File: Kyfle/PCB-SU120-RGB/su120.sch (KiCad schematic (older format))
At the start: 79 parts, among them J1 MJ-4PP-9, J2 Conn_01x03, J3 Conn_01x08, J4 Conn_01x08, J6 MJ-4PP-9, J7 Conn_02x05_Odd_Even, J8 Conn_02x05_Odd_Even, SW1 SW_PUSH_LED, SW10 SW_PUSH_LED, SW11 SW_PUSH_LED, SW12 SW_PUSH_LED, SW13 SW_PUSH_LED, SW14 SW_PUSH_LED, SW15 SW_PUSH_LED, SW16 SW_PUSH_LED, SW17 SW_PUSH_LED, SW18 SW_PUSH_LED, SW2 SW_PUSH_LED, SW20 Rotary_Encoder_Switch, SW21 Rotary_Encoder_Switch, SW22 SW_Push, SW3 SW_PUSH_LED, SW4 SW_PUSH_LED, SW5 SW_PUSH_LED, SW6 SW_PUSH_LED, SW7 SW_PUSH_LED, SW8 SW_PUSH_LED, SW9 SW_PUSH_LED, U1 ProMicro

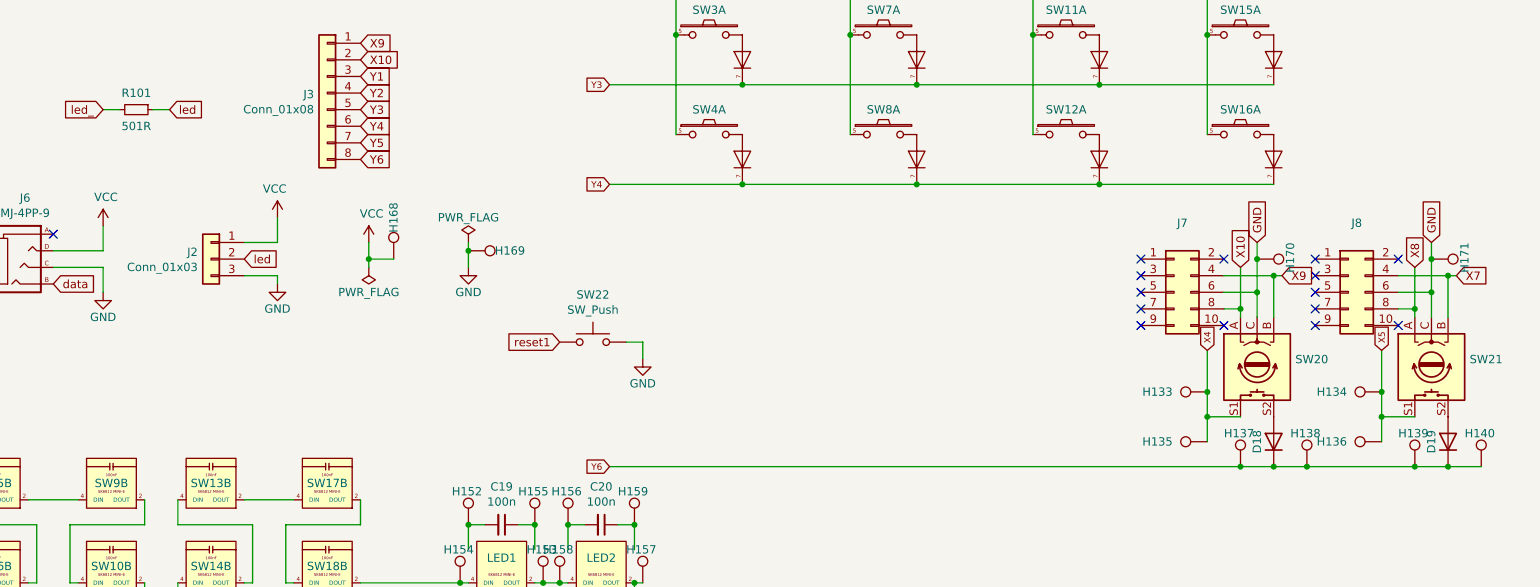
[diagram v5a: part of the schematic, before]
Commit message: PCB done. Started redoing the rails.
- PCB should be in its final version now, pretty much. I hope...
- I added a tentative compatibility with Panasonic roller encoders.
- Also added some silk screens for the 2u stabilisers.
- Propagated the new bit board design to footprints used for top and bottom plate.
- And started to rework the rails in the bottom plate, as well as the general shape of the keyboard.
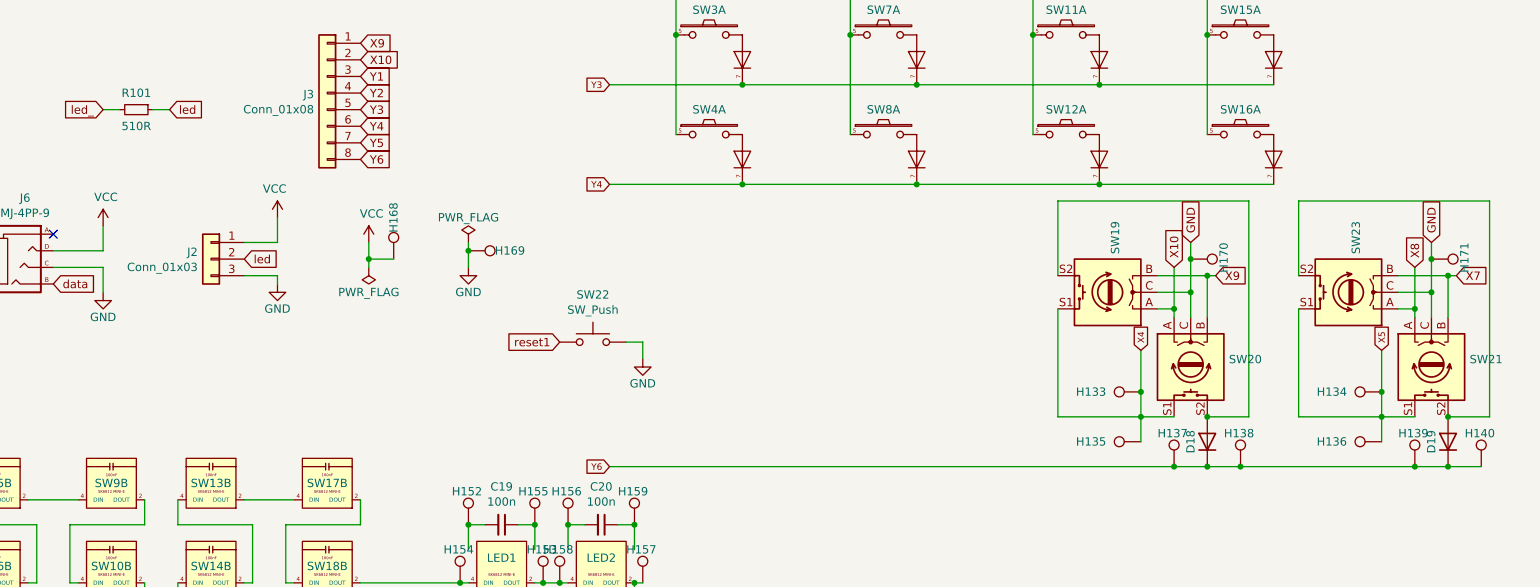
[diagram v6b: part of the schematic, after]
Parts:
- removed J7, J8: Conn_02x05_Odd_Even, #footprint:IDC-Header_2x05_P2.54mm_Vertical, symbol Connector_Generic:Conn_02x05_Odd_Even
- added SW19, SW23: Rotary_Encoder_Switch, Kyfle Footprints:RollerEncoder_Panasonic_EVQWGD001, symbol Device:Rotary_Encoder_Switch
- R101: value 501R -> 510R
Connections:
- net GND: now also SW19.C, SW23.C
- net X10: now also SW19.A
- net X4: now also SW19.S1
- net X5: now also SW23.S1
- net X7: now also SW23.B
- net X8: now also SW23.A
- net X9: now also SW19.B
- net at D18.2 (A), SW20.S2: now also SW19.S2
- net at D19.2 (A), SW21.S2: now also SW23.S2
- no-connect marks 18 -> 4
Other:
- moved on the sheet: D18, H133, H135, H137, H138, H170, SW20
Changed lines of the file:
@@
 L Device:D D18
 U 1 1 5CE5B1E1
-P 9600 5350
-F 0 "D18" H 9600 5450 50  0000 C CNN
-F 1 "D" H 9600 5250 50  0001 C CNN
-F 2 "#footprint:diode_TH_SMD_rev2" H 9600 5350 50  0001 C CNN
-F 3 "" H 9600 5350 50  0001 C CNN
-	1    9600 5350
+P 9200 5350
+F 0 "D18" H 9200 5450 50  0000 C CNN
+F 1 "D" H 9200 5250 50  0001 C CNN
+F 2 "#footprint:diode_TH_SMD_rev2" H 9200 5350 50  0001 C CNN
+F 3 "" H 9200 5350 50  0001 C CNN
+	1    9200 5350
 	0    -1   -1   0
 $EndComp
@@
 Text GLabel 8150 800  1    39   Input ~ 0
 X3
-Text GLabel 9200 4800 1    39   Input ~ 0
+Text GLabel 8800 4800 1    39   Input ~ 0
 X4
 Text GLabel 10250 4800 1    39   Input ~ 0
 X5
-Connection ~ 9600 5500
-Wire Wire Line
-	9600 5500 9800 5500
+Connection ~ 9200 5500
+Wire Wire Line
+	9200 5500 9400 5500
 $Comp
 L Connector:TestPoint H137
 U 1 1 5CE5B292
+P 9000 5500
+F 0 "H137" H 8900 5700 50  0000 L CNN
+F 1 "MountingHole_Pad" H 9100 5460 50  0001 L CNN
+F 2 "#footprint:1pad_conn" H 9000 5500 50  0001 C CNN
+F 3 "~" H 9000 5500 50  0001 C CNN
+	1    9000 5500
+	1    0    0    -1
+$EndComp
+Connection ~ 9000 5500
+Wire Wire Line
+	9000 5500 9200 5500
+$Comp
+L Connector:TestPoint H138
+U 1 1 5CE5B29A
 P 9400 5500
-F 0 "H137" H 9300 5700 50  0000 L CNN
+F 0 "H138" H 9300 5700 50  0000 L CNN
 F 1 "MountingHole_Pad" H 9500 5460 50  0001 L CNN
 F 2 "#footprint:1pad_conn" H 9400 5500 50  0001 C CNN
@@
 Connection ~ 9400 5500
 Wire Wire Line
-	9400 5500 9600 5500
-$Comp
-L Connector:TestPoint H138
-U 1 1 5CE5B29A
-P 9800 5500
-F 0 "H138" H 9700 5700 50  0000 L CNN
-F 1 "MountingHole_Pad" H 9900 5460 50  0001 L CNN
-F 2 "#footprint:1pad_conn" H 9800 5500 50  0001 C CNN
-F 3 "~" H 9800 5500 50  0001 C CNN
-	1    9800 5500
-	1    0    0    -1
-$EndComp
-Connection ~ 9800 5500
-Wire Wire Line
-	9800 5500 10450 5500
+	9400 5500 10450 5500
 $Comp
 L Connector:TestPoint H139
@@
 	1    0    0    -1
 $EndComp
-Connection ~ 10450 5500
-Wire Wire Line
-	10450 5500 10650 5500
 $Comp
 L Connector:TestPoint H140
@@
 L Connector:TestPoint H133
 U 1 1 5CE5B2B0
-P 9200 5050
-F 0 "H133" V 9200 5350 50  0000 C CNN
-F 1 "MountingHole_Pad" V 9346 5055 50  0001 C CNN
-F 2 "#footprint:1pad_conn" H 9200 5050 50  0001 C CNN
-F 3 "~" H 9200 5050 50  0001 C CNN
-	1    9200 5050
+P 8800 5050
+F 0 "H133" V 8800 5350 50  0000 C CNN
+F 1 "MountingHole_Pad" V 8946 5055 50  0001 C CNN
+F 2 "#footprint:1pad_conn" H 8800 5050 50  0001 C CNN
+F 3 "~" H 8800 5050 50  0001 C CNN
+	1    8800 5050
 	0    -1   -1   0
 $EndComp
-Connection ~ 9200 5050
+Connection ~ 8800 5050
 $Comp
 L Connector:TestPoint H135
 U 1 1 5CE5B2B8
-P 9200 5350
-F 0 "H135" V 9200 5650 50  0000 C CNN
-F 1 "MountingHole_Pad" V 9346 5355 50  0001 C CNN
-F 2 "#footprint:1pad_conn" H 9200 5350 50  0001 C CNN
-F 3 "~" H 9200 5350 50  0001 C CNN
-	1    9200 5350
+P 8800 5350
+F 0 "H135" V 8800 5650 50  0000 C CNN
+F 1 "MountingHole_Pad" V 8946 5355 50  0001 C CNN
+F 2 "#footprint:1pad_conn" H 8800 5350 50  0001 C CNN
+F 3 "~" H 8800 5350 50  0001 C CNN
+	1    8800 5350
 	0    -1   -1   0
 $EndComp
@@
 $EndComp
 Wire Wire Line
-	5600 5500 9400 5500
+	5600 5500 9000 5500
 Wire Wire Line
 	10250 4800 10250 5050
 Wire Wire Line
-	9200 4800 9200 5050
-Wire Wire Line
-	9200 5050 9200 5200
+	8800 4800 8800 5050
+Wire Wire Line
+	8800 5050 8800 5200
 Wire Wire Line
 	10250 5050 10250 5200
-$Comp
-L Device:Rotary_Encoder_Switch SW20
-U 1 1 5D659111
-P 9500 4900
-F 0 "SW20" V 9454 4670 50  0000 R CNN
-F 1 "Rotary_Encoder_Switch" V 9545 4670 50  0001 R CNN
-F 2 "#footprint:RotaryEncoder_Alps_EC11E-Switch_Vertical_H20mm_rev2" H 9350 5060 50  0001 C CNN
-F 3 "~" H 9500 5160 50  0001 C CNN
-	1    9500 4900
-	0    -1   1    0
-$EndComp
 $Comp
 L Device:Rotary_Encoder_Switch SW21
@@
 $EndComp
 Wire Wire Line
-	9400 5200 9200 5200
-Connection ~ 9200 5200
-Wire Wire Line
-	9200 5200 9200 5350
+	9000 5200 8800 5200
+Connection ~ 8800 5200
+Wire Wire Line
+	8800 5200 8800 5350
 Wire Wire Line
 	10450 5200 10250 5200
@@
 Wire Wire Line
 	10250 5200 10250 5350
-Text GLabel 9500 4150 1    50   Input ~ 0
+Text GLabel 9100 4150 1    50   Input ~ 0
 GND
 Text GLabel 10550 4150 1    50   Input ~ 0
@@
 	1    0    0    -1
 $EndComp
-$Comp
-L Connector_Generic:Conn_02x05_Odd_Even J8
-U 1 1 5E124F08
-P 10050 4450
-F 0 "J8" H 10100 4867 50  0000 C CNN
-F 1 "Conn_02x05_Odd_Even" H 10100 4776 50  0001 C CNN
-F 2 "#footprint:IDC-Header_2x05_P2.54mm_Vertical" H 10050 4450 50  0001 C CNN
-F 3 "~" H 10050 4450 50  0001 C CNN
-	1    10050 4450
-	1    0    0    -1
-$EndComp
-$Comp
-L Connector_Generic:Conn_02x05_Odd_Even J7
-U 1 1 5E113B23
-P 9000 4450
-F 0 "J7" H 9050 4867 50  0000 C CNN
-F 1 "Conn_02x05_Odd_Even" H 9050 4776 50  0001 C CNN
-F 2 "#footprint:IDC-Header_2x05_P2.54mm_Vertical" H 9000 4450 50  0001 C CNN
-F 3 "~" H 9000 4450 50  0001 C CNN
-	1    9000 4450
-	1    0    0    -1
-$EndComp
-Wire Wire Line
-	9400 4300 9400 4550
-Wire Wire Line
-	9500 4150 9500 4250
+Wire Wire Line
+	9000 4300 9000 4550
+Wire Wire Line
+	9100 4150 9100 4250
 Wire Wire Line
 	10450 4300 10450 4550
@@
 	10550 4150 10550 4250
 Wire Wire Line
-	9300 4350 9600 4350
-Wire Wire Line
-	9600 4350 9600 4600
-Wire Wire Line
-	9300 4450 9500 4450
-Connection ~ 9500 4450
-Wire Wire Line
-	9500 4450 9500 4600
-Wire Wire Line
-	9300 4550 9400 4550
-Connection ~ 9400 4550
-Wire Wire Line
-	9400 4550 9400 4600
+	8900 4350 9200 4350
+Wire Wire Line
+	9200 4350 9200 4600
+Wire Wire Line
+	8900 4450 9100 4450
+Connection ~ 9100 4450
+Wire Wire Line
+	9100 4450 9100 4600
+Wire Wire Line
+	8900 4550 9000 4550
+Connection ~ 9000 4550
+Wire Wire Line
+	9000 4550 9000 4600
 Wire Wire Line
 	10350 4350 10650 4350
@@
 	1    0    0    -1
 $EndComp
-NoConn ~ 8800 4250
-NoConn ~ 8800 4350
-NoConn ~ 8800 4450
-NoConn ~ 8800 4550
-NoConn ~ 8800 4650
-NoConn ~ 9300 4650
-NoConn ~ 9300 4250
-NoConn ~ 9850 4250
-NoConn ~ 9850 4350
-NoConn ~ 9850 4450
-NoConn ~ 9850 4550
-NoConn ~ 9850 4650
-NoConn ~ 10350 4650
-NoConn ~ 10350 4250
 $Comp
 L Sofle:SW_PUSH_LED SW4
@@
 P 2750 3350
 F 0 "R101" V 2650 3350 50  0000 C CNN
-F 1 "501R" V 2850 3350 50  0000 C CNN
+F 1 "510R" V 2850 3350 50  0000 C CNN
 F 2 "Resistor_SMD:R_0603_1608Metric_Pad0.98x0.95mm_HandSolder" H 2750 3350 50  0001 C CNN
 F 3 "~" H 2750 3350 50  0001 C CNN
@@
 Wire Wire Line
 	2650 3350 2550 3350
-Connection ~ 9600 4350
+Connection ~ 9200 4350
 Wire Wire Line
 	10700 4350 10650 4350
@@
 L Connector:TestPoint H170
 U 1 1 617932EC
-P 9500 4250
-F 0 "H170" H 9400 4450 50  0000 L CNN
-F 1 "MountingHole_Pad" H 9600 4210 50  0001 L CNN
-F 2 "#footprint:1pin_conn" H 9500 4250 50  0001 C CNN
-F 3 "~" H 9500 4250 50  0001 C CNN
-	1    9500 4250
+P 9100 4250
+F 0 "H170" H 9000 4450 50  0000 L CNN
+F 1 "MountingHole_Pad" H 9200 4210 50  0001 L CNN
+F 2 "#footprint:1pin_conn" H 9100 4250 50  0001 C CNN
+F 3 "~" H 9100 4250 50  0001 C CNN
+	1    9100 4250
 	0    1    1    0
 $EndComp
-Connection ~ 9500 4250
-Wire Wire Line
-	9500 4250 9500 4450
+Connection ~ 9100 4250
+Wire Wire Line
+	9100 4250 9100 4450
 $Comp
 L Connector:TestPoint H171
@@
 	4750 4200 4750 4300
 Wire Wire Line
-	9650 4350 9600 4350
-Text GLabel 9650 4350 2    50   Input ~ 0
-X9
-Text GLabel 9400 4300 1    50   Input ~ 0
+	9250 4350 9200 4350
+Text GLabel 9000 4300 1    50   Input ~ 0
 X10
 Text GLabel 3450 1900 2    50   Input ~ 0
@@
 Text GLabel 3400 4250 2    50   Input ~ 0
 led
+$Comp
+L Device:Rotary_Encoder_Switch SW20
+U 1 1 5D659111
+P 9100 4900
+F 0 "SW20" V 9054 4670 50  0000 R CNN
+F 1 "Rotary_Encoder_Switch" V 9145 4670 50  0001 R CNN
+F 2 "#footprint:RotaryEncoder_Alps_EC11E-Switch_Vertical_H20mm_rev2" H 8950 5060 50  0001 C CNN
+F 3 "~" H 9100 5160 50  0001 C CNN
+	1    9100 4900
+	0    -1   1    0
+$EndComp
+Text GLabel 9250 4350 2    50   Input ~ 0
+X9
+$Comp
+L Device:Rotary_Encoder_Switch SW19
+U 1 1 617B91CB
+P 8600 4450
+F 0 "SW19" V 8554 4220 50  0000 R CNN
+F 1 "Rotary_Encoder_Switch" V 8645 4220 50  0001 R CNN
+F 2 "Kyfle Footprints:RollerEncoder_Panasonic_EVQWGD001" H 8450 4610 50  0001 C CNN
+F 3 "~" H 8600 4710 50  0001 C CNN
+	1    8600 4450
+	-1   0    0    1
+$EndComp
+Wire Wire Line
+	8300 4550 8300 5200
+Wire Wire Line
+	8300 5200 8800 5200
+Connection ~ 9200 5200
+Wire Wire Line
+	8300 4350 8300 3900
+Wire Wire Line
+	8300 3900 9450 3900
+Wire Wire Line
+	9450 3900 9450 5200
+Wire Wire Line
+	9450 5200 9200 5200
+$Comp
+L Device:Rotary_Encoder_Switch SW23
+U 1 1 617D6B8F
+P 10050 4450
+F 0 "SW23" V 10004 4220 50  0000 R CNN
+F 1 "Rotary_Encoder_Switch" V 10095 4220 50  0001 R CNN
+F 2 "Kyfle Footprints:RollerEncoder_Panasonic_EVQWGD001" H 9900 4610 50  0001 C CNN
+F 3 "~" H 10050 4710 50  0001 C CNN
+	1    10050 4450
+	-1   0    0    1
+$EndComp
+Connection ~ 10450 5500
+Wire Wire Line
+	10450 5500 10650 5500
+Wire Wire Line
+	9750 4550 9750 5200
+Wire Wire Line
+	9750 5200 10250 5200
+Wire Wire Line
+	9750 4350 9750 3900
+Wire Wire Line
+	9750 3900 10900 3900
+Wire Wire Line
+	10900 3900 10900 5200
+Wire Wire Line
+	10900 5200 10650 5200
+Connection ~ 10650 5200
 $EndSCHEMATC

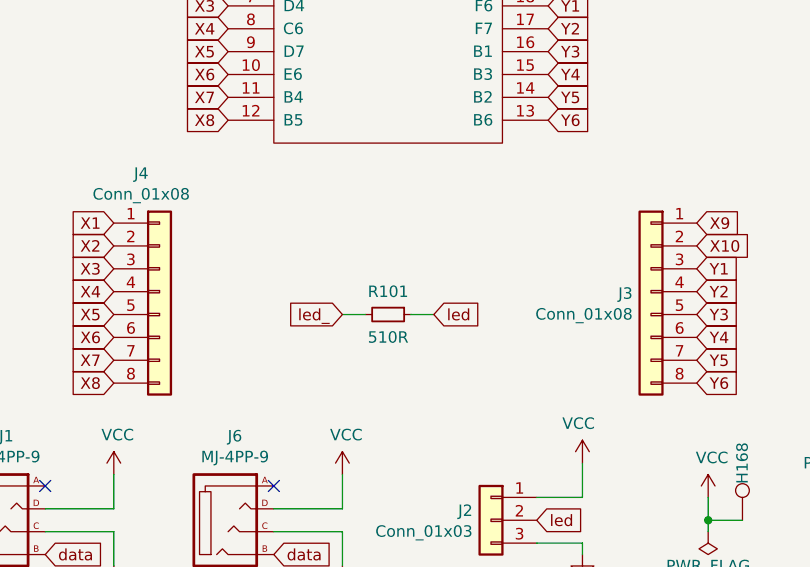
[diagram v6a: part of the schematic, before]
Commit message: Finalized main PCB
- After receiving rivets hardware, they are actually not holding onto the pin headers ... M1.1 rivets would be needed, but they are barely available and cost a lot more.
- So instead of using rivets, we will use female pin headers (the "lowest profile" ones but still widely standard), but using 1.5mm holes such that they sunk into the board more and gets even lower profile (~2.8mm, instead of +4mm)
- So the pro micro footprint did not change, has it already had 1.5mm holes. But OLED footprint changed for more classic 0.8mm holes as in this case we can use the added thickness of the pin header to offset the OLED board higher up.
- Also finally routed VCC from pro micro board to the rest
- And extended pro micro board 2mm in length to make room for the top M2 mount holes while still providing enough board surface to squeeze onto.
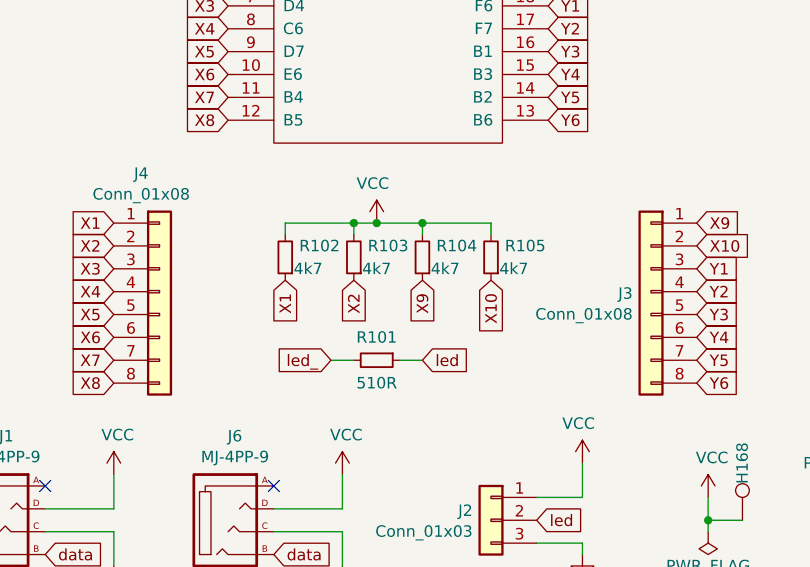
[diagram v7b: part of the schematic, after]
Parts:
- added R102, R103, R104, R105: 4k7, Resistor_SMD:R_0603_1608Metric_Pad0.98x0.95mm_HandSolder, symbol Device:R_Small
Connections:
- net VCC: now also R102.2, R103.2, R104.2, R105.2
- net X1: now also R102.1
- net X10: now also R105.1
- net X2: now also R103.1
- net X9: now also R104.1
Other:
- moved on the sheet: R101
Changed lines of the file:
@@
 	-1   0    0    -1
 $EndComp
-Text GLabel 2950 3350 2    50   Input ~ 0
+Text GLabel 2900 3550 2    50   Input ~ 0
 led
 Text GLabel 1250 4400 2    50   Input ~ 0
@@
 L Device:R_Small R101
 U 1 1 62335352
-P 2750 3350
-F 0 "R101" V 2650 3350 50  0000 C CNN
-F 1 "510R" V 2850 3350 50  0000 C CNN
-F 2 "Resistor_SMD:R_0603_1608Metric_Pad0.98x0.95mm_HandSolder" H 2750 3350 50  0001 C CNN
-F 3 "~" H 2750 3350 50  0001 C CNN
-	1    2750 3350
+P 2700 3550
+F 0 "R101" V 2600 3550 50  0000 C CNN
+F 1 "510R" V 2800 3550 50  0000 C CNN
+F 2 "Resistor_SMD:R_0603_1608Metric_Pad0.98x0.95mm_HandSolder" H 2700 3550 50  0001 C CNN
+F 3 "~" H 2700 3550 50  0001 C CNN
+	1    2700 3550
 	0    1    1    0
 $EndComp
 Wire Wire Line
-	2950 3350 2850 3350
-Wire Wire Line
-	2650 3350 2550 3350
+	2900 3550 2800 3550
+Wire Wire Line
+	2600 3550 2500 3550
 Connection ~ 9200 4350
 Wire Wire Line
@@
 Wire Wire Line
 	5750 7050 5800 7050
-Text GLabel 2550 3350 0    50   Input ~ 0
+Text GLabel 2500 3550 0    50   Input ~ 0
 led_
 Text GLabel 3400 4250 2    50   Input ~ 0
@@
 	10900 5200 10650 5200
 Connection ~ 10650 5200
+$Comp
+L Device:R_Small R102
+U 1 1 617E22EC
+P 2300 3100
+F 0 "R102" H 2150 3050 50  0000 C CNN
+F 1 "4k7" H 2200 3150 50  0000 C CNN
+F 2 "Resistor_SMD:R_0603_1608Metric_Pad0.98x0.95mm_HandSolder" H 2300 3100 50  0001 C CNN
+F 3 "~" H 2300 3100 50  0001 C CNN
+	1    2300 3100
+	-1   0    0    1
+$EndComp
+$Comp
+L Device:R_Small R103
+U 1 1 617F9D27
+P 2600 3100
+F 0 "R103" H 2450 3050 50  0000 C CNN
+F 1 "4k7" H 2500 3150 50  0000 C CNN
+F 2 "Resistor_SMD:R_0603_1608Metric_Pad0.98x0.95mm_HandSolder" H 2600 3100 50  0001 C CNN
+F 3 "~" H 2600 3100 50  0001 C CNN
+	1    2600 3100
+	-1   0    0    1
+$EndComp
+$Comp
+L Device:R_Small R104
+U 1 1 617F9F3F
+P 2900 3100
+F 0 "R104" H 2750 3050 50  0000 C CNN
+F 1 "4k7" H 2800 3150 50  0000 C CNN
+F 2 "Resistor_SMD:R_0603_1608Metric_Pad0.98x0.95mm_HandSolder" H 2900 3100 50  0001 C CNN
+F 3 "~" H 2900 3100 50  0001 C CNN
+	1    2900 3100
+	-1   0    0    1
+$EndComp
+$Comp
+L Device:R_Small R105
+U 1 1 617FA297
+P 3200 3100
+F 0 "R105" H 3050 3050 50  0000 C CNN
+F 1 "4k7" H 3100 3150 50  0000 C CNN
+F 2 "Resistor_SMD:R_0603_1608Metric_Pad0.98x0.95mm_HandSolder" H 3200 3100 50  0001 C CNN
+F 3 "~" H 3200 3100 50  0001 C CNN
+	1    3200 3100
+	-1   0    0    1
+$EndComp
+$Comp
+L power:VCC #PWR0105
+U 1 1 618067A2
+P 2700 2950
+F 0 "#PWR0105" H 2700 2800 50  0001 C CNN
+F 1 "VCC" H 2717 3123 50  0000 C CNN
+F 2 "" H 2700 2950 50  0001 C CNN
+F 3 "" H 2700 2950 50  0001 C CNN
+	1    2700 2950
+	-1   0    0    -1
+$EndComp
+Text GLabel 2300 3200 3    50   Input ~ 0
+X1
+Text GLabel 2600 3200 3    50   Input ~ 0
+X2
+Wire Wire Line
+	2300 3000 2300 2950
+Wire Wire Line
+	2300 2950 2600 2950
+Wire Wire Line
+	2700 2950 2900 2950
+Wire Wire Line
+	3200 2950 3200 3000
+Connection ~ 2700 2950
+Wire Wire Line
+	2900 3000 2900 2950
+Connection ~ 2900 2950
+Wire Wire Line
+	2900 2950 3200 2950
+Wire Wire Line
+	2600 3000 2600 2950
+Connection ~ 2600 2950
+Wire Wire Line
+	2600 2950 2700 2950
+Text GLabel 2900 3200 3    50   Input ~ 0
+X9
+Text GLabel 3200 3200 3    50   Input ~ 0
+X10
 $EndSCHEMATC
